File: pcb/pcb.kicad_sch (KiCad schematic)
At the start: 1 part

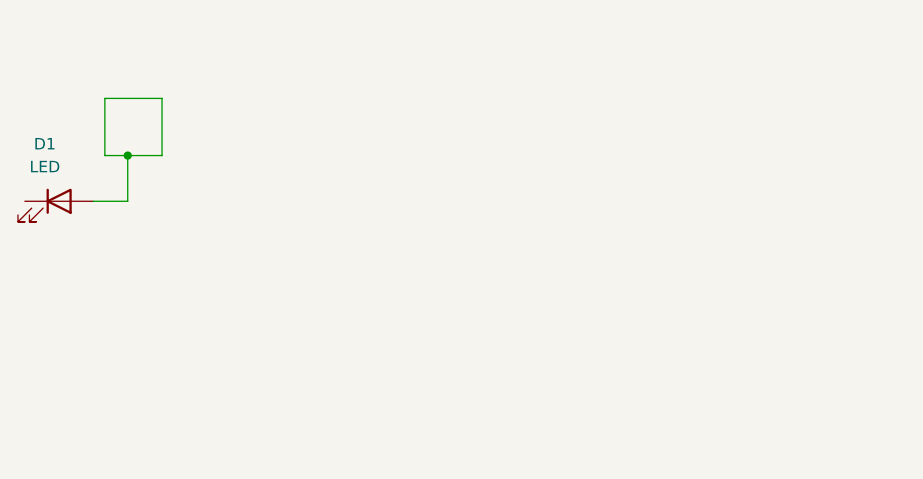
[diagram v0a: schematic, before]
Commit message: add multiplexer symbol
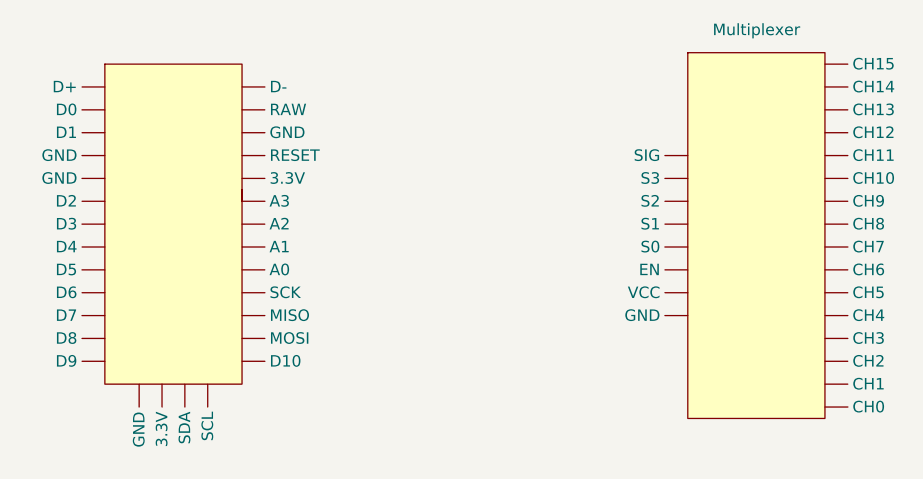
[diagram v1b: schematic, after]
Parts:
- removed D1: LED, symbol Device:LED
- added KB2040: ~, symbol KB2040:KB2040
- added Multiplexer: ~, symbol analog_multiplexer:multiplexer
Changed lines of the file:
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@@
 (kicad_sch (version 20230121) (generator eeschema)
   (paper "A4")
-  (junction (at 101.6 86.36) (diameter 0) (color 0 0 0 0)
-  )
-  (wire (pts (xy 101.6 86.36) (xy 105.41 86.36))
-    (stroke (width 0) (type default))
-  )
-  (wire (pts (xy 101.6 86.36) (xy 99.06 86.36))
-    (stroke (width 0) (type default))
-  )
-  (wire (pts (xy 99.06 80.01) (xy 105.41 80.01))
-    (stroke (width 0) (type default))
-  )
-  (wire (pts (xy 105.41 80.01) (xy 105.41 86.36))
-    (stroke (width 0) (type default))
-  )
-  (wire (pts (xy 97.79 91.44) (xy 101.6 91.44))
-    (stroke (width 0) (type default))
-  )
-  (wire (pts (xy 99.06 86.36) (xy 99.06 80.01))
-    (stroke (width 0) (type default))
-  )
-  (wire (pts (xy 101.6 91.44) (xy 101.6 86.36))
-    (stroke (width 0) (type default))
-  )
-  (symbol (lib_id "Device:LED") (at 93.98 91.44 0) (unit 1)
+  (symbol (lib_id "KB2040:KB2040") (at 106.68 92.71 0) (unit 1)
     (in_bom yes) (on_board yes) (dnp no) (fields_autoplaced)
-    (property "Reference" "D1" (at 92.3925 85.09 0)
+    (property "Reference" "KB2040" (at 106.68 116.84 0)
+      (effects (font (size 1.27 1.27)) hide)
+    )
+    (property "Value" "~" (at 120.65 87.63 0)
       (effects (font (size 1.27 1.27)))
     )
-    (property "Value" "LED" (at 92.3925 87.63 0)
-      (effects (font (size 1.27 1.27)))
-    )
-    (property "Footprint" "" (at 93.98 91.44 0)
+    (property "Footprint" "" (at 120.65 87.63 0)
       (effects (font (size 1.27 1.27)) hide)
     )
-    (property "Datasheet" "~" (at 93.98 91.44 0)
+    (property "Datasheet" "" (at 120.65 87.63 0)
       (effects (font (size 1.27 1.27)) hide)
     )
-    (pin "2")
-    (pin "1")
+    (pin "")
+    (pin "")
+    (pin "")
+    (pin "")
+    (pin "")
+    (pin "")
+    (pin "")
+    (pin "")
+    (pin "")
+    (pin "")
+    (pin "")
+    (pin "")
+    (pin "")
+    (pin "")
+    (pin "")
+    (pin "")
+    (pin "")
+    (pin "")
+    (pin "")
+    (pin "")
+    (pin "")
+    (pin "")
+    (pin "")
+    (pin "")
+    (pin "")
+    (pin "")
+    (pin "")
+    (pin "")
+    (pin "")
+    (pin "")
     (instances
       (project "pcb"
         (path "/7cd41366-658c-4c64-bfa9-b0a6b780fad4"
-          (reference "D1") (unit 1)
+          (reference "KB2040") (unit 1)
         )
       )
+    )
+  )
+  (symbol (lib_id "analog_multiplexer:multiplexer") (at 171.45 96.52 0) (unit 1)
+    (in_bom yes) (on_board yes) (dnp no) (fields_autoplaced)
+    (property "Reference" "Multiplexer" (at 171.45 72.39 0)
+      (effects (font (size 1.27 1.27)))
+    )
+    (property "Value" "~" (at 170.18 92.71 0)
+      (effects (font (size 1.27 1.27)))
+    )
+    (property "Footprint" "" (at 170.18 92.71 0)
+      (effects (font (size 1.27 1.27)) hide)
+    )
+    (property "Datasheet" "" (at 170.18 92.71 0)
+      (effects (font (size 1.27 1.27)) hide)
+    )
+    (pin "")
+    (pin "")
+    (pin "")
+    (pin "")
+    (pin "")
+    (pin "")
+    (pin "")
+    (pin "")
+    (pin "")
+    (pin "")
+    (pin "")
+    (pin "")
+    (pin "")
+    (pin "")
+    (pin "")
+    (pin "")
+    (pin "")
+    (pin "")
+    (pin "")
+    (pin "")
+    (pin "")
+    (pin "")
+    (pin "")
+    (pin "")
+    (instances
+      (project "pcb"
+        (path "/7cd41366-658c-4c64-bfa9-b0a6b780fad4"
+          (reference "Multiplexer") (unit 1)
+        )
+      )

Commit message: pcb schema
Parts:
- added J1, J10, J11, J12, J13, J14, J15, J16, J17, J18, J19, J2, J20, J3, J4, J5, J6, J7, J8, J9: Conn_02x04_Odd_Even, symbol Connector_Generic:Conn_02x04_Odd_Even
- Multiplexer1: renamed from Multiplexer; value ~ -> mulriplexer
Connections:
- net at KB2040. (SDA): now also Multiplexer1. (VCC)
- net GND: now reaches Multiplexer1. (VCC)
- net GND: now also J1.1 (Pin_1), J10.1 (Pin_1), J11.1 (Pin_1), J12.1 (Pin_1), J13.1 (Pin_1), J14.1 (Pin_1), J15.1 (Pin_1), J16.1 (Pin_1), J17.1 (Pin_1), J18.1 (Pin_1), J19.1 (Pin_1), J2.1 (Pin_1), J20.1 (Pin_1), J3.1 (Pin_1), J4.1 (Pin_1), J5.1 (Pin_1), J6.1 (Pin_1), J7.1 (Pin_1), J8.1 (Pin_1), J9.1 (Pin_1)
- new net: J10.4 (Pin_4), J14.4 (Pin_4), J18.4 (Pin_4), J2.4 (Pin_4), J6.4 (Pin_4), KB2040. (SDA)
- new net: J13.6 (Pin_6), J14.6 (Pin_6), J15.6 (Pin_6), J16.6 (Pin_6), KB2040. (SDA)
- new net: J1.7 (Pin_7), J10.7 (Pin_7), J11.7 (Pin_7), J12.7 (Pin_7), J13.7 (Pin_7), J14.7 (Pin_7), J15.7 (Pin_7), J16.7 (Pin_7), J17.7 (Pin_7), J18.7 (Pin_7), J19.7 (Pin_7), J2.7 (Pin_7), J20.7 (Pin_7), J3.7 (Pin_7), J4.7 (Pin_7), J5.7 (Pin_7), J6.7 (Pin_7), J7.7 (Pin_7), J8.7 (Pin_7), J9.7 (Pin_7), KB2040. (SDA)
- new net: J1.8 (Pin_8), J10.8 (Pin_8), J11.8 (Pin_8), J12.8 (Pin_8), J13.8 (Pin_8), J14.8 (Pin_8), J15.8 (Pin_8), J16.8 (Pin_8), J17.8 (Pin_8), J18.8 (Pin_8), J19.8 (Pin_8), J2.8 (Pin_8), J20.8 (Pin_8), J3.8 (Pin_8), J4.8 (Pin_8), J5.8 (Pin_8), J6.8 (Pin_8), J7.8 (Pin_8), J8.8 (Pin_8), J9.8 (Pin_8), KB2040. (SDA)
- new net: J5.6 (Pin_6), J6.6 (Pin_6), J7.6 (Pin_6), J8.6 (Pin_6), KB2040. (SDA)
- new net: J10.6 (Pin_6), J11.6 (Pin_6), J12.6 (Pin_6), J9.6 (Pin_6), KB2040. (SDA)
- new net: J1.4 (Pin_4), J13.4 (Pin_4), J17.4 (Pin_4), J5.4 (Pin_4), J9.4 (Pin_4), KB2040. (SDA)
- new net: J12.4 (Pin_4), J16.4 (Pin_4), J20.4 (Pin_4), J4.4 (Pin_4), J8.4 (Pin_4), KB2040. (SDA)
- new net: J17.6 (Pin_6), J18.6 (Pin_6), J19.6 (Pin_6), J20.6 (Pin_6), KB2040. (SDA)
- new net: J1.6 (Pin_6), J2.6 (Pin_6), J3.6 (Pin_6), J4.6 (Pin_6), KB2040. (SDA)
- new net: J11.4 (Pin_4), J15.4 (Pin_4), J19.4 (Pin_4), J3.4 (Pin_4), J7.4 (Pin_4), KB2040. (SDA)
- new net: KB2040. (SDA), Multiplexer1. (VCC) (x4)
- new net: J14.3 (Pin_3), Multiplexer1. (VCC)
- new net: J6.3 (Pin_3), Multiplexer1. (VCC)
- new net: J10.3 (Pin_3), Multiplexer1. (VCC)
- new net: J5.3 (Pin_3), Multiplexer1. (VCC)
- new net: J12.3 (Pin_3), Multiplexer1. (VCC)
- new net: J20.3 (Pin_3), Multiplexer1. (VCC)
- new net: J13.3 (Pin_3), Multiplexer1. (VCC)
- new net: J18.3 (Pin_3), Multiplexer1. (VCC)
- new net: J7.3 (Pin_3), Multiplexer1. (VCC)
- new net: J11.3 (Pin_3), Multiplexer1. (VCC)
- new net: J17.3 (Pin_3), Multiplexer1. (VCC)
- new net: J16.3 (Pin_3), Multiplexer1. (VCC)
- new net: J15.3 (Pin_3), Multiplexer1. (VCC)
- new net: J9.3 (Pin_3), Multiplexer1. (VCC)
- new net: J8.3 (Pin_3), Multiplexer1. (VCC)
- new net: J19.3 (Pin_3), Multiplexer1. (VCC)
- new net +3.3V: J1.2 (Pin_2), J10.2 (Pin_2), J11.2 (Pin_2), J12.2 (Pin_2), J13.2 (Pin_2), J14.2 (Pin_2), J15.2 (Pin_2), J16.2 (Pin_2), J17.2 (Pin_2), J18.2 (Pin_2), J19.2 (Pin_2), J2.2 (Pin_2), J20.2 (Pin_2), J3.2 (Pin_2), J4.2 (Pin_2), J5.2 (Pin_2), J6.2 (Pin_2), J7.2 (Pin_2), J8.2 (Pin_2), J9.2 (Pin_2), Multiplexer1. (VCC)
- no-connect marks 0 -> 24
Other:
- moved on the sheet: Multiplexer1

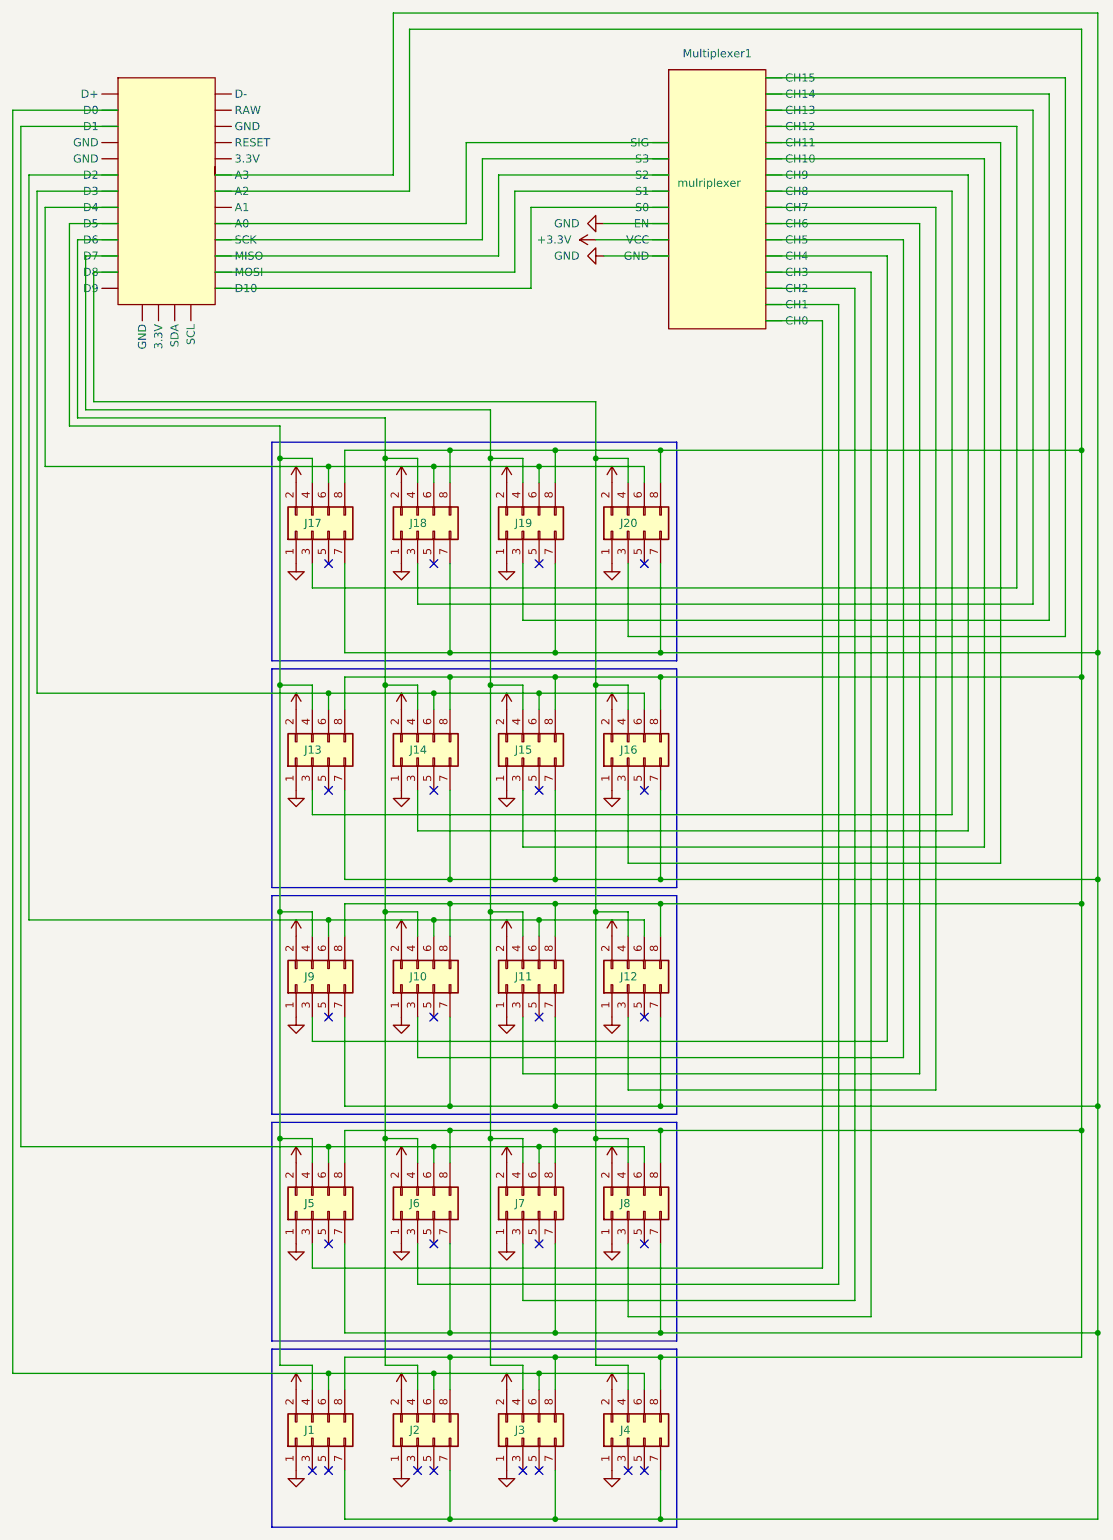
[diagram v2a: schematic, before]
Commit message: fixed pin rotation on custom components
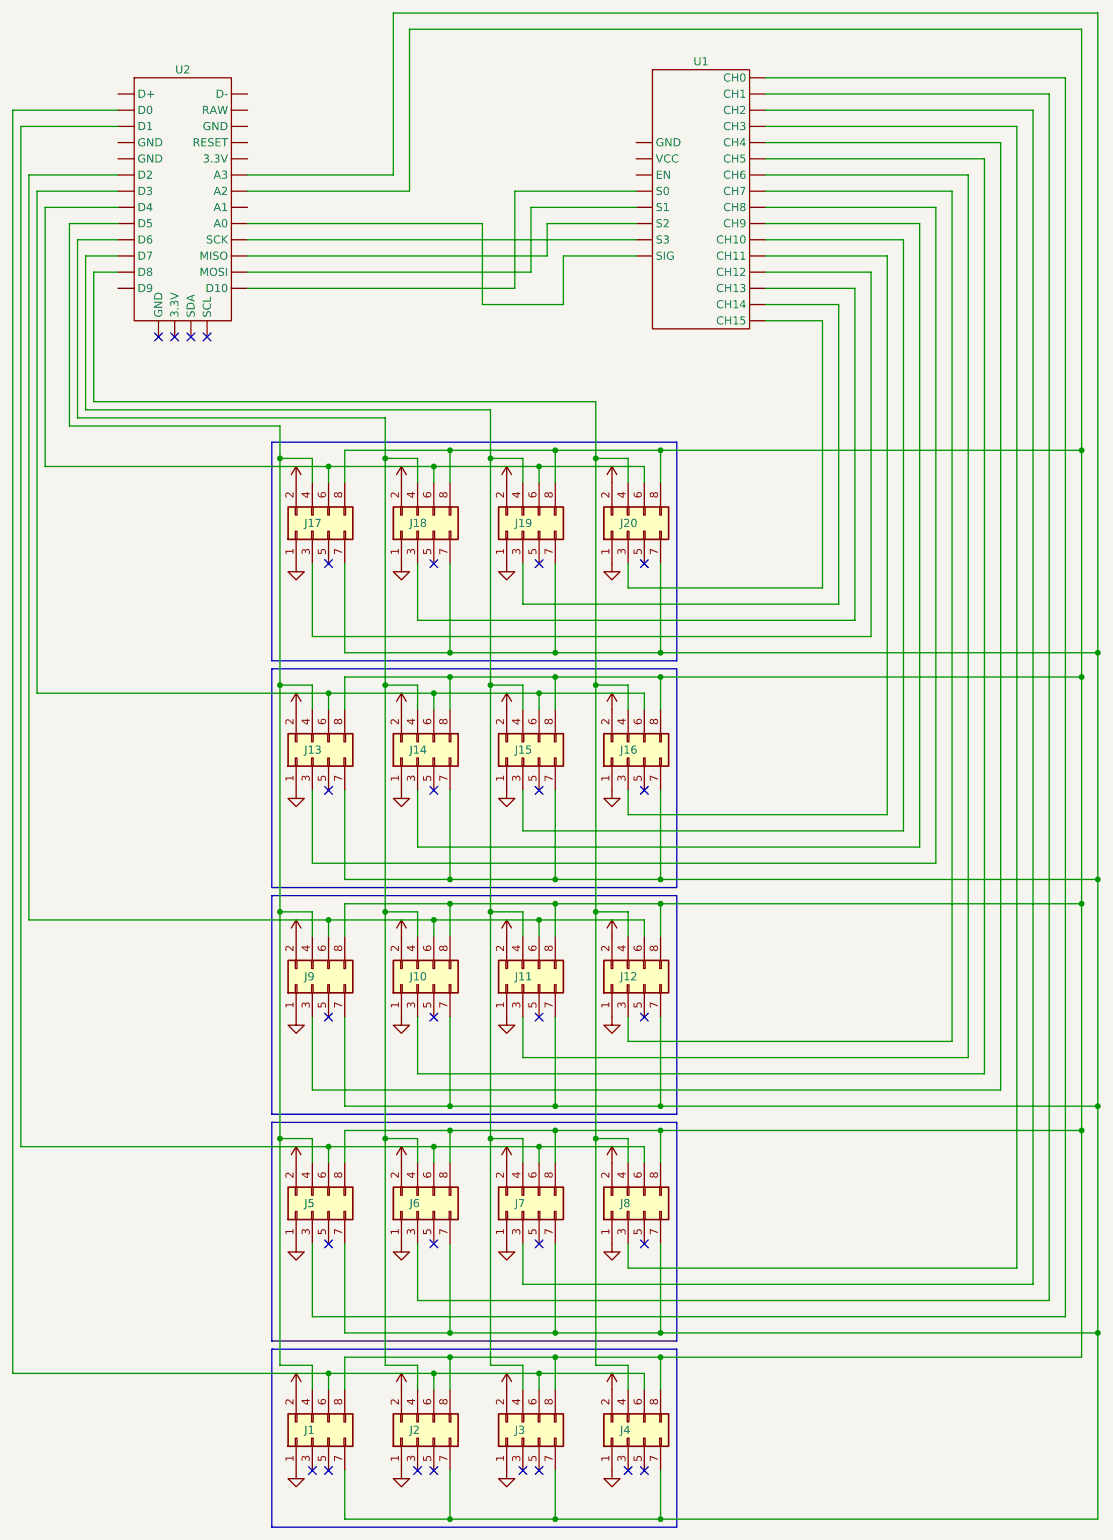
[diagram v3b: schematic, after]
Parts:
- removed KB2040: ~, symbol KB2040:KB2040
- removed Multiplexer1: mulriplexer, symbol analog_multiplexer:multiplexer
- added U1: ~, symbol analog_multiplexer:multiplexer
- added U2: ~, symbol KB2040:KB2040
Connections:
- net at J10.4 (Pin_4), J14.4 (Pin_4), J18.4 (Pin_4)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: now also U2. (SDA)
- net at J13.6 (Pin_6), J14.6 (Pin_6), J15.6 (Pin_6)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: now also U2. (SDA)
- net at J1.7 (Pin_7), J10.7 (Pin_7), J11.7 (Pin_7)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: now also U2. (SDA)
- net at J1.8 (Pin_8), J10.8 (Pin_8), J11.8 (Pin_8)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: now also U2. (SDA)
- net at J5.6 (Pin_6), J6.6 (Pin_6), J7.6 (Pin_6)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: now also U2. (SDA)
- net at J10.6 (Pin_6), J11.6 (Pin_6), J12.6 (Pin_6)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: now also U2. (SDA)
- net at J1.4 (Pin_4), J13.4 (Pin_4), J17.4 (Pin_4)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: now also U2. (SDA)
- net at J12.4 (Pin_4), J16.4 (Pin_4), J20.4 (Pin_4)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: now also U2. (SDA)
- net at J17.6 (Pin_6), J18.6 (Pin_6), J19.6 (Pin_6)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: now also U2. (SDA)
- net at J1.6 (Pin_6), J2.6 (Pin_6), J3.6 (Pin_6)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: now also U2. (SDA)
- net at J11.4 (Pin_4), J15.4 (Pin_4), J19.4 (Pin_4)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: now also U2. (SDA)
- net at J14.3 (Pin_3): now also U1. (VCC)
- net at J6.3 (Pin_3): now also U1. (VCC)
- net at J10.3 (Pin_3): now also U1. (VCC)
- net at J5.3 (Pin_3): now also U1. (VCC)
- net at J12.3 (Pin_3): now also U1. (VCC)
- net at J20.3 (Pin_3): now also U1. (VCC)
- net at J13.3 (Pin_3): now also U1. (VCC)
- net at J18.3 (Pin_3): now also U1. (VCC)
- net at J7.3 (Pin_3): now also U1. (VCC)
- net at J11.3 (Pin_3): now also U1. (VCC)
- net at J17.3 (Pin_3): now also U1. (VCC)
- net at J16.3 (Pin_3): now also U1. (VCC)
- net at J15.3 (Pin_3): now also U1. (VCC)
- net at J9.3 (Pin_3): now also U1. (VCC)
- net at J8.3 (Pin_3): now also U1. (VCC)
- net at J19.3 (Pin_3): now also U1. (VCC)
- new net: U1. (VCC), U2. (SDA) (x5)
- no-connect marks 24 -> 28

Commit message: add pcb footprints to pin headers
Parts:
- removed U2: ~, symbol KB2040:KB2040
- added J21: Conn_01x04_Pin, Connector_PinHeader_2.54mm:PinHeader_1x04_P2.54mm_Vertical, symbol Connector:Conn_01x04_Pin
- added U3: ~, symbol KB2040:KB2040
- J1, J10, J11, J12, J13, J14, J15, J16, J17, J18, J19, J2, J20, J3, J4, J5, J6, J7, J8, J9: footprint (none) -> Connector_PinHeader_2.54mm:PinHeader_2x04_P2.54mm_Vertical
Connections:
- net +3.3V: now also U1. (VCC), U3. (SDA)
- net GND: now also U1. (VCC), U3. (SDA)
- net at J10.4 (Pin_4), J14.4 (Pin_4), J18.4 (Pin_4)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: now also U3. (SDA)
- net at J13.6 (Pin_6), J14.6 (Pin_6), J15.6 (Pin_6)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: now also U3. (SDA)
- net at J1.7 (Pin_7), J10.7 (Pin_7), J11.7 (Pin_7)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: now also U3. (SDA)
- net at J1.8 (Pin_8), J10.8 (Pin_8), J11.8 (Pin_8)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: now also U3. (SDA)
- net at J5.6 (Pin_6), J6.6 (Pin_6), J7.6 (Pin_6)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: now also U3. (SDA)
- net at J10.6 (Pin_6), J11.6 (Pin_6), J12.6 (Pin_6)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: now also U3. (SDA)
- net at J1.4 (Pin_4), J13.4 (Pin_4), J17.4 (Pin_4)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: now also U3. (SDA)
- net at J12.4 (Pin_4), J16.4 (Pin_4), J20.4 (Pin_4)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: now also U3. (SDA)
- net at J17.6 (Pin_6), J18.6 (Pin_6), J19.6 (Pin_6)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: now also U3. (SDA)
- net at J1.6 (Pin_6), J2.6 (Pin_6), J3.6 (Pin_6)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: now also U3. (SDA)
- net at J11.4 (Pin_4), J15.4 (Pin_4), J19.4 (Pin_4)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: now also U3. (SDA)
- new net: J21.1 (Pin_1), U3. (SDA)
- new net: J21.2 (Pin_2), U3. (SDA)
- new net: J21.3 (Pin_3), U3. (SDA)
- new net: J21.4 (Pin_4), U3. (SDA)
- new net: U1. (VCC), U3. (SDA) (x5)
- no-connect marks 28 -> 30
